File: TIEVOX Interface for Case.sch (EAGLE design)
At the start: 23 parts, among them U4 CAT24C32.UDFN8

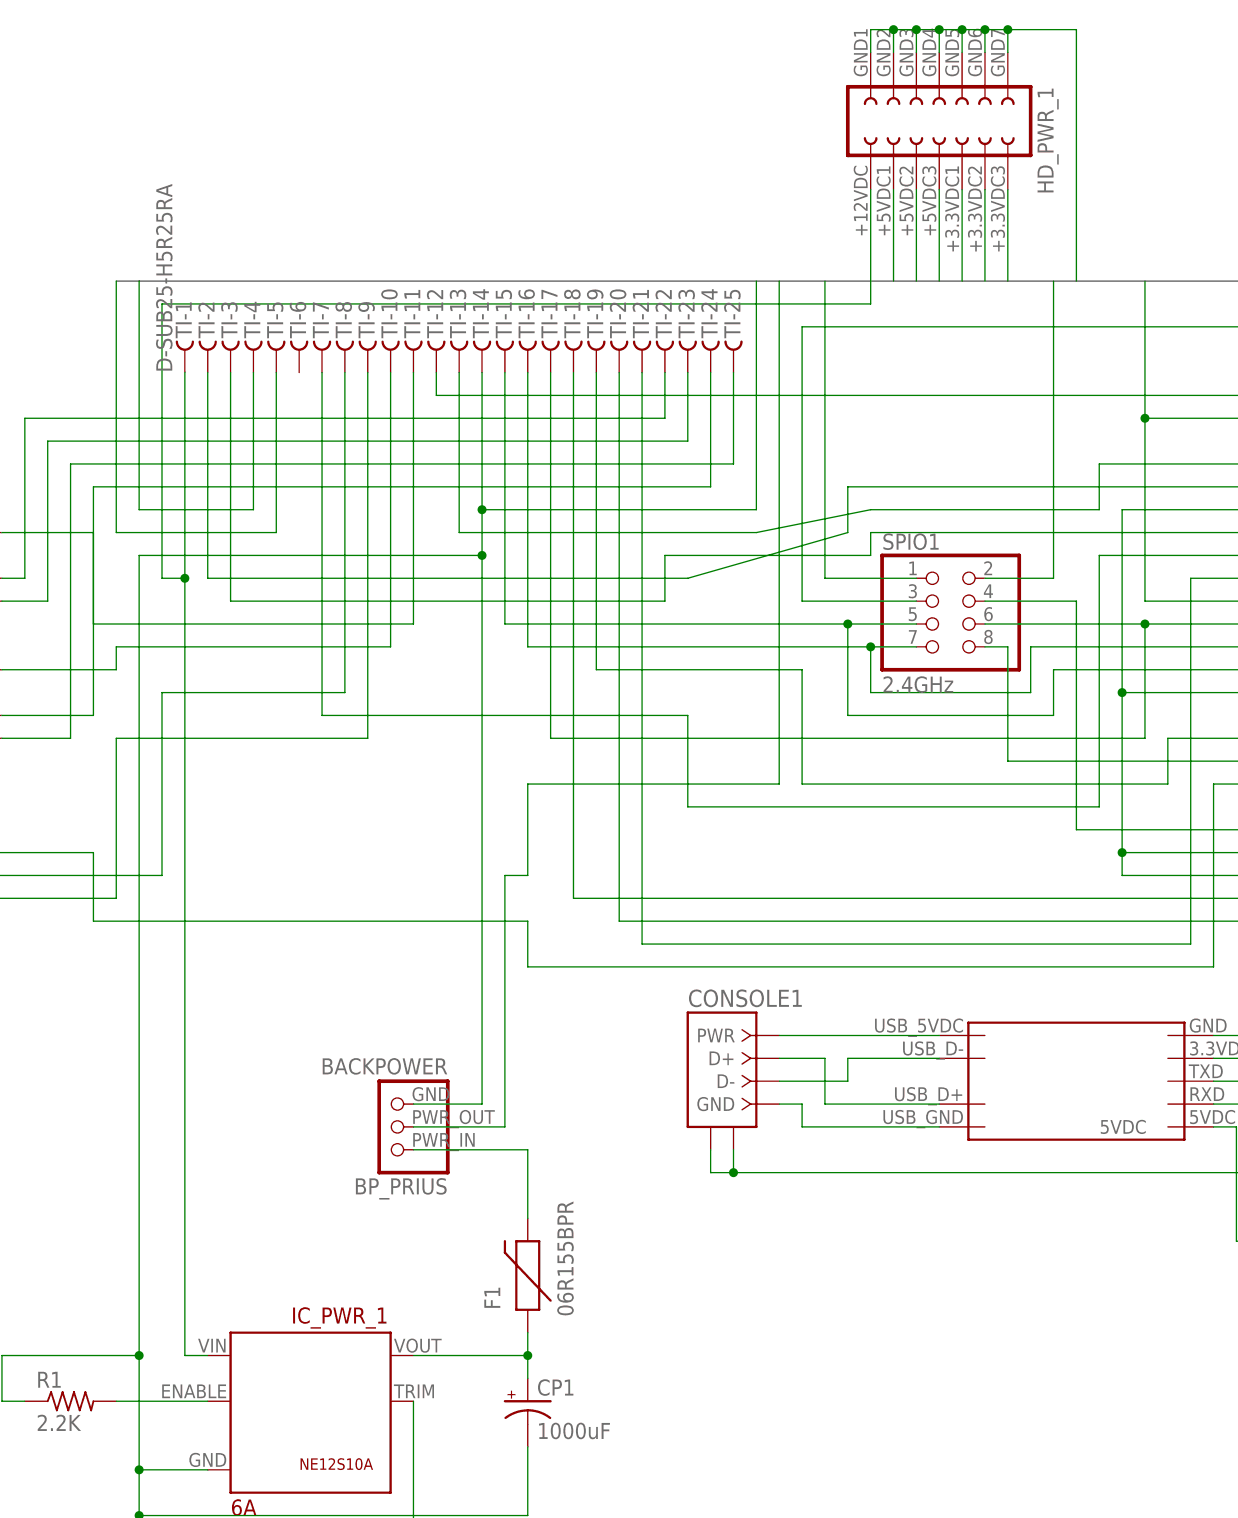
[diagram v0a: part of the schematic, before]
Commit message: Removed power header. Not sure that it's needed, and need to see if that'll help get everything routed.
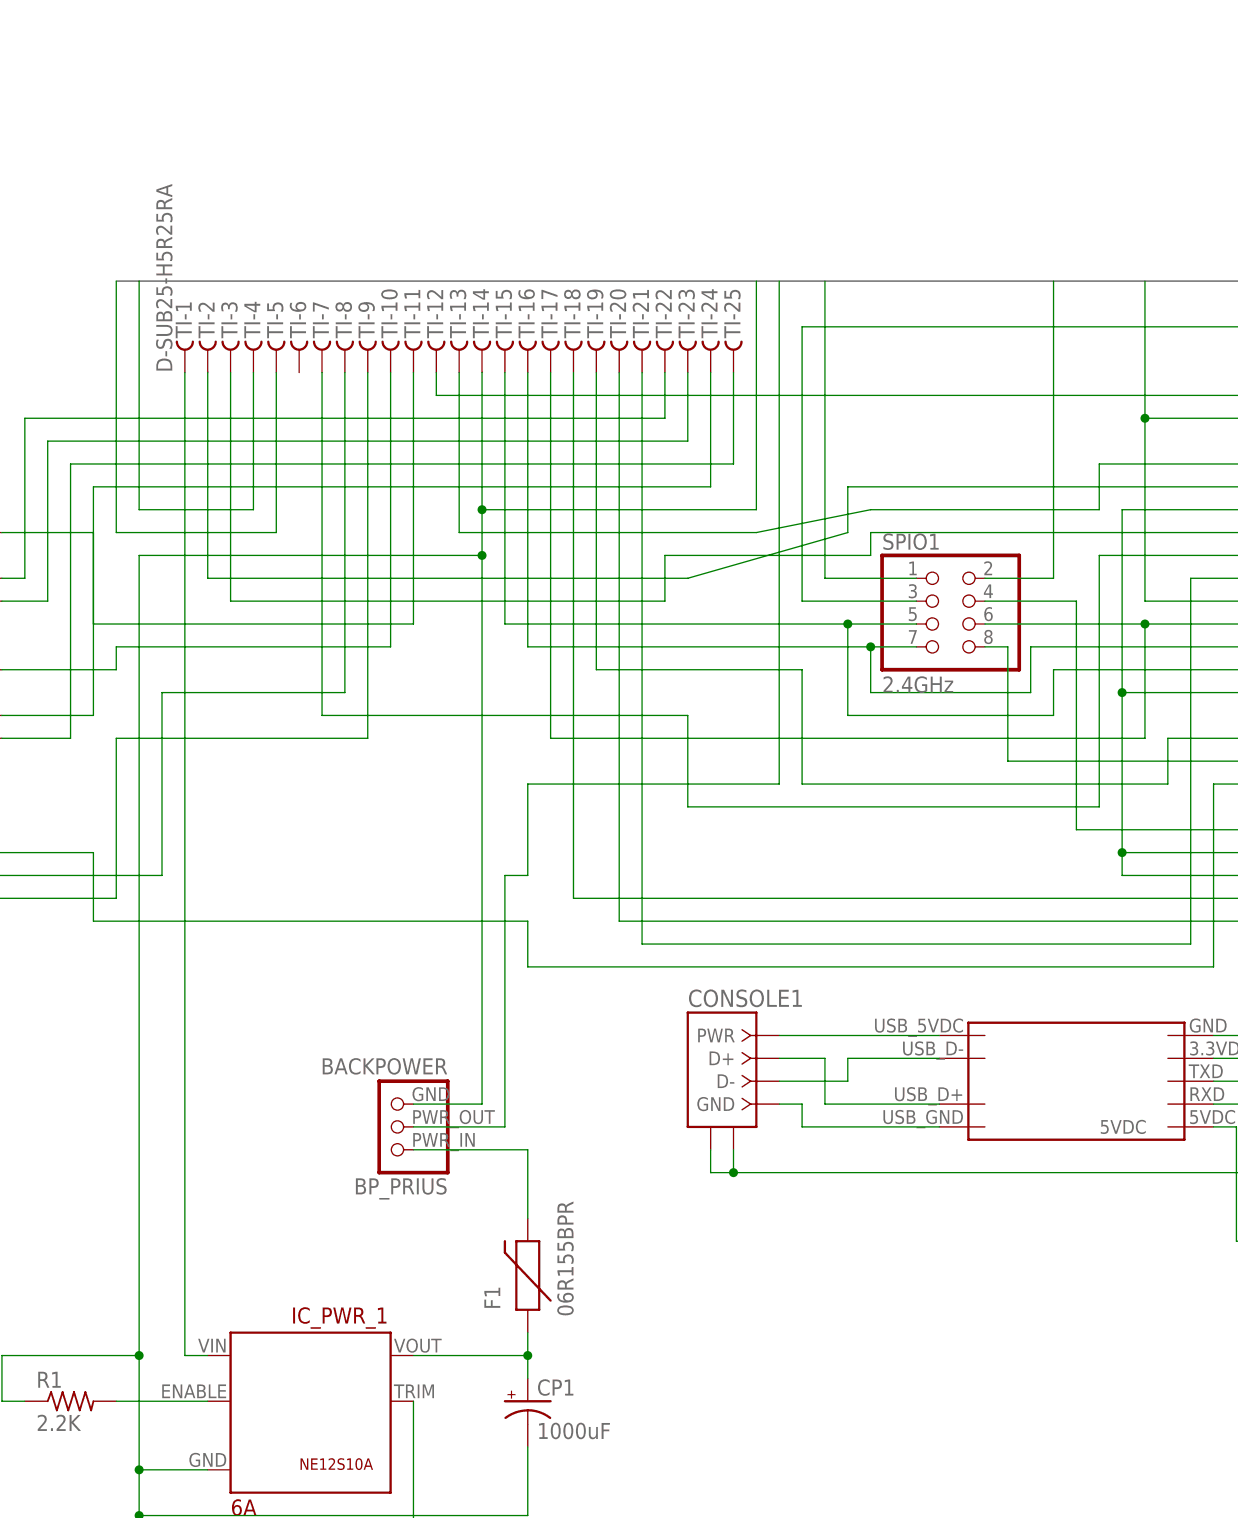
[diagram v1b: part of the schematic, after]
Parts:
- removed HD_PWR_1: PWR_HDR_FEMALE_2X7, con-lsta:PWR_HDR_FEMALE_2X7
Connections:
- net +3.3VDC: no longer HD_PWR_1.10, HD_PWR_1.12, HD_PWR_1.14
- net +5VDC: no longer HD_PWR_1.4, HD_PWR_1.6, HD_PWR_1.8
- net GND: no longer HD_PWR_1.1, HD_PWR_1.11, HD_PWR_1.13, HD_PWR_1.3, HD_PWR_1.5, HD_PWR_1.7, HD_PWR_1.9
- net PWR12_IN: no longer HD_PWR_1.2
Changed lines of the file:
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@@
 <part name="CP1" library="rcl" deviceset="CPOL-US" device="E3.5-8" value="1000uF"/>
 <part name="IC_PWR_1" library="packages" deviceset="NE12S*" device="12V6A" value="6A"/>
-<part name="HD_PWR_1" library="con-lsta" deviceset="PWR_HDR_FEMALE_2X7" device=""/>
 <part name="SPIO1" library="pinhead" deviceset="PINHD-2X4" device="" value="2.4GHz"/>
 <part name="UART1" library="packages" deviceset="GS27159" device=""/>
@@
 <instance part="CP1" gate="G$1" x="30.48" y="-27.94"/>
 <instance part="IC_PWR_1" gate="G$1" x="0" y="-27.94"/>
-<instance part="HD_PWR_1" gate="G$1" x="76.2" y="114.3" rot="R270"/>
 <instance part="SPIO1" gate="A" x="76.2" y="58.42"/>
 <instance part="UART1" gate="G$1" x="91.44" y="7.62" rot="R270"/>
@@
 <wire x1="17.78" y1="2.54" x2="27.94" y2="2.54" width="0.1524" layer="91"/>
 <wire x1="27.94" y1="2.54" x2="27.94" y2="30.48" width="0.1524" layer="91"/>
-</segment>
-<segment>
-<pinref part="HD_PWR_1" gate="G$1" pin="4"/>
-<wire x1="71.12" y1="96.52" x2="71.12" y2="106.68" width="0.1524" layer="91"/>
-</segment>
-<segment>
-<pinref part="HD_PWR_1" gate="G$1" pin="6"/>
-<wire x1="73.66" y1="96.52" x2="73.66" y2="106.68" width="0.1524" layer="91"/>
-</segment>
-<segment>
-<pinref part="HD_PWR_1" gate="G$1" pin="8"/>
-<wire x1="76.2" y1="96.52" x2="76.2" y2="106.68" width="0.1524" layer="91"/>
 </segment>
 <segment>
@@
 </segment>
 <segment>
-<wire x1="91.44" y1="96.52" x2="91.44" y2="124.46" width="0.1524" layer="91"/>
-<wire x1="91.44" y1="124.46" x2="83.82" y2="124.46" width="0.1524" layer="91"/>
-<pinref part="HD_PWR_1" gate="G$1" pin="1"/>
-<wire x1="83.82" y1="124.46" x2="81.28" y2="124.46" width="0.1524" layer="91"/>
-<wire x1="81.28" y1="124.46" x2="78.74" y2="124.46" width="0.1524" layer="91"/>
-<wire x1="78.74" y1="124.46" x2="76.2" y2="124.46" width="0.1524" layer="91"/>
-<wire x1="76.2" y1="124.46" x2="73.66" y2="124.46" width="0.1524" layer="91"/>
-<wire x1="73.66" y1="124.46" x2="71.12" y2="124.46" width="0.1524" layer="91"/>
-<wire x1="71.12" y1="124.46" x2="68.58" y2="124.46" width="0.1524" layer="91"/>
-<wire x1="68.58" y1="124.46" x2="68.58" y2="121.92" width="0.1524" layer="91"/>
-<pinref part="HD_PWR_1" gate="G$1" pin="3"/>
-<wire x1="71.12" y1="121.92" x2="71.12" y2="124.46" width="0.1524" layer="91"/>
-<junction x="71.12" y="124.46"/>
-<pinref part="HD_PWR_1" gate="G$1" pin="5"/>
-<wire x1="73.66" y1="121.92" x2="73.66" y2="124.46" width="0.1524" layer="91"/>
-<junction x="73.66" y="124.46"/>
-<pinref part="HD_PWR_1" gate="G$1" pin="7"/>
-<wire x1="76.2" y1="121.92" x2="76.2" y2="124.46" width="0.1524" layer="91"/>
-<junction x="76.2" y="124.46"/>
-<pinref part="HD_PWR_1" gate="G$1" pin="9"/>
-<wire x1="78.74" y1="124.46" x2="78.74" y2="121.92" width="0.1524" layer="91"/>
-<junction x="78.74" y="124.46"/>
-<pinref part="HD_PWR_1" gate="G$1" pin="11"/>
-<wire x1="81.28" y1="124.46" x2="81.28" y2="121.92" width="0.1524" layer="91"/>
-<junction x="81.28" y="124.46"/>
-<pinref part="HD_PWR_1" gate="G$1" pin="13"/>
-<wire x1="83.82" y1="124.46" x2="83.82" y2="121.92" width="0.1524" layer="91"/>
-<junction x="83.82" y="124.46"/>
-</segment>
-<segment>
 <pinref part="U4" gate="G$1" pin="GND"/>
 <wire x1="190.5" y1="55.88" x2="170.18" y2="55.88" width="0.1524" layer="91"/>
@@
 <wire x1="81.28" y1="63.5" x2="88.9" y2="63.5" width="0.1524" layer="91"/>
 <wire x1="88.9" y1="63.5" x2="88.9" y2="96.52" width="0.1524" layer="91"/>
-</segment>
-<segment>
-<pinref part="HD_PWR_1" gate="G$1" pin="10"/>
-<wire x1="78.74" y1="96.52" x2="78.74" y2="106.68" width="0.1524" layer="91"/>
-</segment>
-<segment>
-<pinref part="HD_PWR_1" gate="G$1" pin="12"/>
-<wire x1="81.28" y1="96.52" x2="81.28" y2="106.68" width="0.1524" layer="91"/>
-</segment>
-<segment>
-<pinref part="HD_PWR_1" gate="G$1" pin="14"/>
-<wire x1="83.82" y1="96.52" x2="83.82" y2="106.68" width="0.1524" layer="91"/>
 </segment>
 <segment>
@@
 <segment>
 <pinref part="TI" gate="-1" pin="F"/>
-<wire x1="-7.62" y1="86.36" x2="-7.62" y2="63.5" width="0.1524" layer="91"/>
 <pinref part="IC_PWR_1" gate="G$1" pin="VIN"/>
-<wire x1="-7.62" y1="63.5" x2="-7.62" y2="-22.86" width="0.1524" layer="91"/>
+<wire x1="-7.62" y1="86.36" x2="-7.62" y2="-22.86" width="0.1524" layer="91"/>
 <wire x1="-7.62" y1="-22.86" x2="-5.08" y2="-22.86" width="0.1524" layer="91"/>
-<wire x1="-7.62" y1="63.5" x2="-10.16" y2="63.5" width="0.1524" layer="91"/>
-<wire x1="-10.16" y1="63.5" x2="-10.16" y2="93.98" width="0.1524" layer="91"/>
-<junction x="-7.62" y="63.5"/>
-<wire x1="-10.16" y1="93.98" x2="68.58" y2="93.98" width="0.1524" layer="91"/>
-<pinref part="HD_PWR_1" gate="G$1" pin="2"/>
-<wire x1="68.58" y1="93.98" x2="68.58" y2="106.68" width="0.1524" layer="91"/>
-</segment>
-</net>
+</segment>
+</net>

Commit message: Removed extraneous ground and +VDC connections to GPIO to aid in routing.
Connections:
- net +3.3VDC: no longer GPIO1.17_3.3VDC
- net +5VDC: no longer GPIO1.4_5VDC
- net GND: no longer GPIO1.20_GND, GPIO1.25_GND, GPIO1.30_GND, GPIO1.34_GND, GPIO1.39_GND, GPIO1.9_GND
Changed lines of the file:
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@@
-</segment>
-<segment>
-<pinref part="GPIO1" gate="G$1" pin="4_5VDC"/>
-<wire x1="137.16" y1="78.74" x2="165.1" y2="78.74" width="0.1524" layer="91"/>
 </segment>
 <segment>
@@
 </segment>
 <segment>
-<pinref part="GPIO1" gate="G$1" pin="20_GND"/>
-<wire x1="137.16" y1="58.42" x2="165.1" y2="58.42" width="0.1524" layer="91"/>
-</segment>
-<segment>
 <pinref part="GPIO1" gate="G$1" pin="14_GND"/>
 <wire x1="137.16" y1="66.04" x2="165.1" y2="66.04" width="0.1524" layer="91"/>
-</segment>
-<segment>
-<pinref part="GPIO1" gate="G$1" pin="34_GND"/>
-<wire x1="137.16" y1="40.64" x2="165.1" y2="40.64" width="0.1524" layer="91"/>
-</segment>
-<segment>
-<wire x1="165.1" y1="30.48" x2="96.52" y2="30.48" width="0.1524" layer="91"/>
-<pinref part="GPIO1" gate="G$1" pin="39_GND"/>
-<wire x1="127" y1="33.02" x2="96.52" y2="33.02" width="0.1524" layer="91"/>
-<pinref part="GPIO1" gate="G$1" pin="25_GND"/>
-<wire x1="96.52" y1="33.02" x2="96.52" y2="50.8" width="0.1524" layer="91"/>
-<wire x1="96.52" y1="50.8" x2="127" y2="50.8" width="0.1524" layer="91"/>
-<pinref part="GPIO1" gate="G$1" pin="9_GND"/>
-<wire x1="96.52" y1="50.8" x2="96.52" y2="71.12" width="0.1524" layer="91"/>
-<wire x1="96.52" y1="71.12" x2="127" y2="71.12" width="0.1524" layer="91"/>
-<junction x="96.52" y="50.8"/>
-<wire x1="96.52" y1="30.48" x2="96.52" y2="33.02" width="0.1524" layer="91"/>
-<junction x="96.52" y="33.02"/>
 </segment>
 <segment>
@@
 <wire x1="73.66" y1="63.5" x2="63.5" y2="63.5" width="0.1524" layer="91"/>
 <wire x1="63.5" y1="63.5" x2="63.5" y2="96.52" width="0.1524" layer="91"/>
-</segment>
-<segment>
-<pinref part="GPIO1" gate="G$1" pin="30_GND"/>
-<wire x1="137.16" y1="45.72" x2="165.1" y2="45.72" width="0.1524" layer="91"/>
 </segment>
 <segment>
@@
 <wire x1="99.06" y1="96.52" x2="99.06" y2="81.28" width="0.1524" layer="91"/>
 <wire x1="99.06" y1="81.28" x2="127" y2="81.28" width="0.1524" layer="91"/>
-<pinref part="GPIO1" gate="G$1" pin="17_3.3VDC"/>
-<wire x1="99.06" y1="81.28" x2="99.06" y2="60.96" width="0.1524" layer="91"/>
-<wire x1="99.06" y1="60.96" x2="127" y2="60.96" width="0.1524" layer="91"/>
-<junction x="99.06" y="81.28"/>
 </segment>
 <segment>

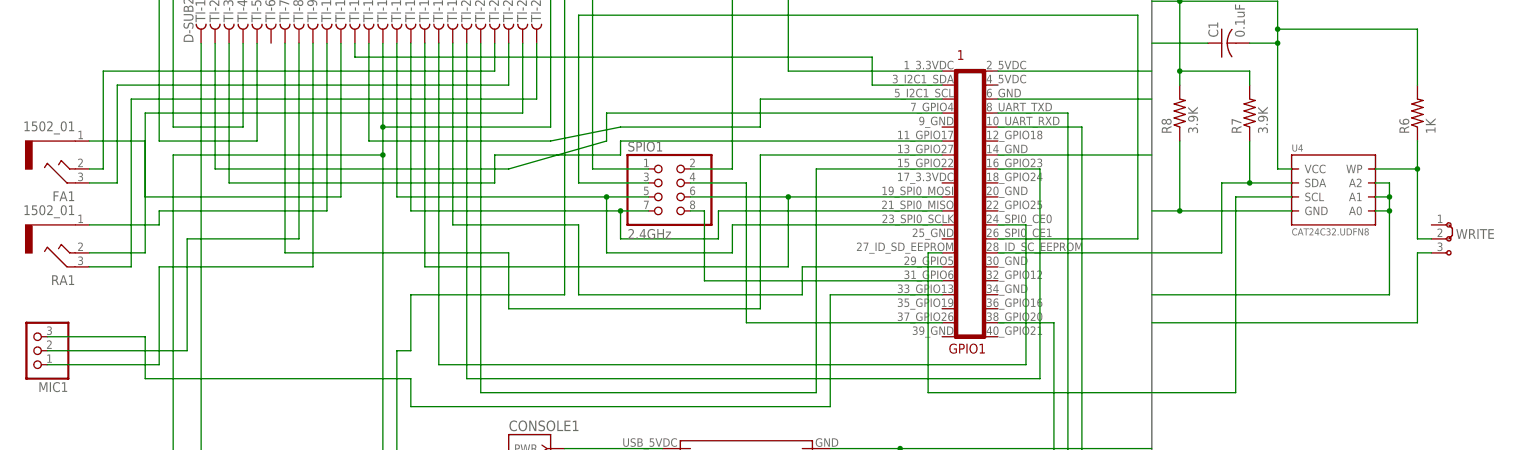
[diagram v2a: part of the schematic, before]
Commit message: Another attempt to build Interface without vias.
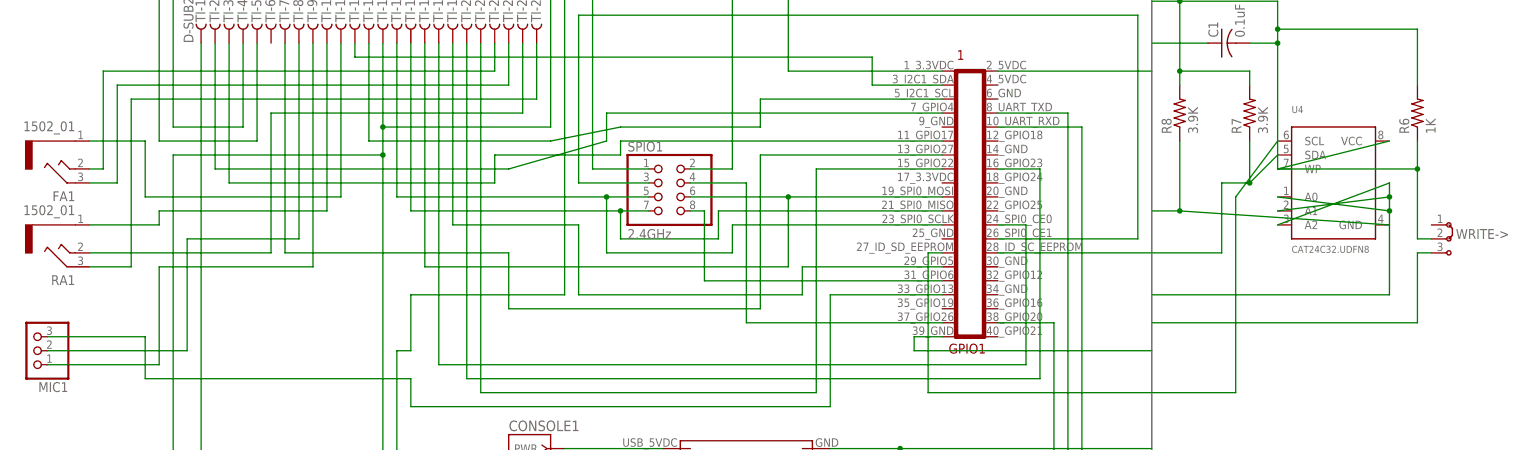
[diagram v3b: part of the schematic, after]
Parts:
- C1: device adafruit:C-USC1005 -> adafruit:C-US025-050X050
- R6, R7, R8: device adafruit:R-US_R1005 -> adafruit:R-US_0207/10
- U4: device on-semiconductor:CAT24CXX.UDFN8 -> microbuilder:EEPROM_I2C_SOIC8_GENERIC
- renumbered WRITE to WRITE->
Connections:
- net GND: now also GPIO1.39_GND; no longer GPIO1.14_GND, GPIO1.6_GND
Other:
- moved on the sheet: U4
